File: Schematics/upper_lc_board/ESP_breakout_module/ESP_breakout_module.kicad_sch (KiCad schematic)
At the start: 28 parts, among them J8 USB_C_Female_USB2_Small, U1 ESP32-S3-WROOM-1-N16R2, U2 CAN_TRX_SN65HVD230DR, U3 PD_D3V3XA4B10LP

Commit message: finish adding components to layout, revise layout next.
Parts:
- removed C4: 0.1uF, Capacitor_SMD:C_0603_1608Metric, symbol Device:C
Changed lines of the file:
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@@
 	(wire
 		(pts
-			(xy 134.62 83.82) (xy 134.62 82.55)
-		)
-		(stroke
-			(width 0)
-			(type default)
-			(color 194 0 0 1)
-		)
-	)
-	(wire
-		(pts
 			(xy 201.93 80.01) (xy 208.28 80.01)
 		)
@@
 	)
 	(symbol
-		(lib_id "Device:C")
-		(at 134.62 78.74 0)
-		(unit 1)
-		(exclude_from_sim no)
-		(in_bom yes)
-		(on_board yes)
-		(dnp no)
-		(property "Reference" "C4"
-			(at 127.762 77.724 0)
-			(effects
-				(font
-					(size 1.27 1.27)
-				)
-				(justify left)
-			)
-		)
-		(property "Value" "0.1uF"
-			(at 127 79.7561 0)
-			(effects
-				(font
-					(size 1.27 1.27)
-				)
-				(justify left)
-			)
-		)
-		(property "Footprint" "Capacitor_SMD:C_0603_1608Metric"
-			(at 135.5852 82.55 0)
-			(effects
-				(font
-					(size 1.27 1.27)
-				)
-				(hide yes)
-			)
-		)
-		(property "Datasheet" "~"
-			(at 134.62 78.74 0)
-			(effects
-				(font
-					(size 1.27 1.27)
-				)
-				(hide yes)
-			)
-		)
-		(property "Description" "Unpolarized capacitor"
-			(at 134.62 78.74 0)
-			(effects
-				(font
-					(size 1.27 1.27)
-				)
-				(hide yes)
-			)
-		)
-		(pin "2"
-		)
-		(pin "1"
-		)
-		(instances
-			(project ""
-				(path "/9b1a1d2a-fad7-4f10-83f3-1f83e9656c75/1d6cfe1a-a78a-448d-9dfa-b2b78f04d682"
-					(reference "C4")
-					(unit 1)
-				)
-			)
-		)
-	)
-	(symbol
-		(lib_id "power:GND")
-		(at 134.62 74.93 180)
-		(unit 1)
-		(exclude_from_sim no)
-		(in_bom yes)
-		(on_board yes)
-		(dnp no)
-		(property "Reference" "#PWR013"
-			(at 134.62 68.58 0)
-			(effects
-				(font
-					(size 1.27 1.27)
-				)
-				(hide yes)
-			)
-		)
-		(property "Value" "GND"
-			(at 134.62 71.882 90)
-			(effects
-				(font
-					(size 1.27 1.27)
-				)
-				(justify right)
-			)
-		)
-		(property "Footprint" ""
-			(at 134.62 74.93 0)
-			(effects
-				(font
-					(size 1.27 1.27)
-				)
-				(hide yes)
-			)
-		)
-		(property "Datasheet" ""
-			(at 134.62 74.93 0)
-			(effects
-				(font
-					(size 1.27 1.27)
-				)
-				(hide yes)
-			)
-		)
-		(property "Description" "Power symbol creates a global label with name \"GND\" , ground"
-			(at 134.62 74.93 0)
-			(effects
-				(font
-					(size 1.27 1.27)
-				)
-				(hide yes)
-			)
-		)
-		(pin "1"
-		)
-		(instances
-			(project ""
-				(path "/9b1a1d2a-fad7-4f10-83f3-1f83e9656c75/1d6cfe1a-a78a-448d-9dfa-b2b78f04d682"
-					(reference "#PWR013")
-					(unit 1)
-				)
-			)
-		)
-	)
-	(symbol
 		(lib_id "Device:R")
 		(at 190.5 68.58 90)
@@
 					(unit 1)
 				)
-			)
-		)
-	)
-	(symbol
-		(lib_id "power:+3V3")
-		(at 134.62 83.82 180)
-		(unit 1)
-		(exclude_from_sim no)
-		(in_bom yes)
-		(on_board yes)
-		(dnp no)
-		(property "Reference" "#PWR012"
-			(at 134.62 80.01 0)
-			(effects
-				(font
-					(size 1.27 1.27)
-				)
-				(hide yes)
-			)
-		)
-		(property "Value" "+3V3"
-			(at 134.62 88.9 90)
-			(effects
-				(font
-					(size 1.27 1.27)
-				)
-			)
-		)
-		(property "Footprint" ""
-			(at 134.62 83.82 0)
-			(effects
-				(font
-					(size 1.27 1.27)
-				)
-				(hide yes)
-			)
-		)
-		(property "Datasheet" ""
-			(at 134.62 83.82 0)
-			(effects
-				(font
-					(size 1.27 1.27)
-				)
-				(hide yes)
-			)
-		)
-		(property "Description" "Power symbol creates a global label with name \"+3V3\""
-			(at 134.62 83.82 0)
-			(effects
-				(font
-					(size 1.27 1.27)
-				)
-				(hide yes)
-			)
-		)
-		(pin "1"
-		)
-		(instances
-			(project ""
-				(path "/9b1a1d2a-fad7-4f10-83f3-1f83e9656c75/1d6cfe1a-a78a-448d-9dfa-b2b78f04d682"
-					(reference "#PWR012")
-					(unit 1)
-				)

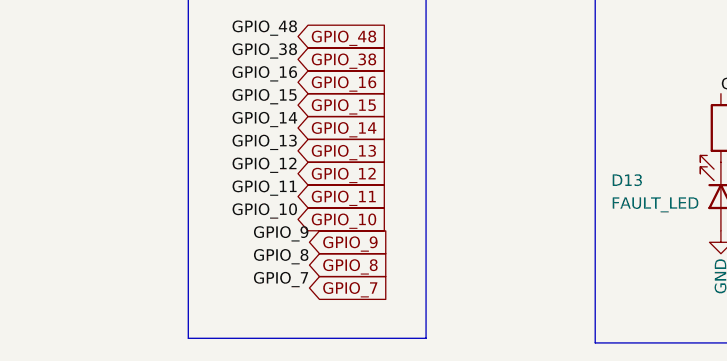
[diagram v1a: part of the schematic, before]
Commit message: add thermistor circuitry & update layout
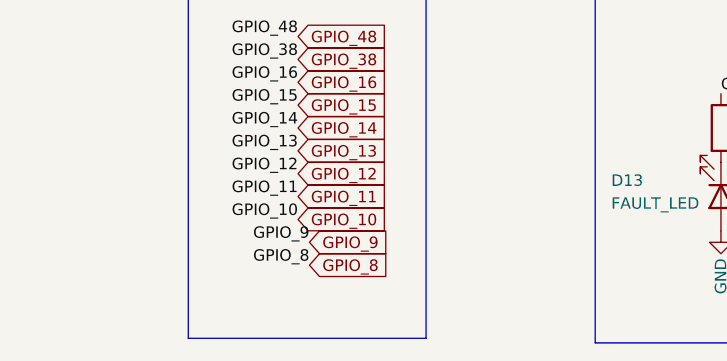
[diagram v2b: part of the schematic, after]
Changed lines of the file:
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@@
-		)
-	)
-	(label "GPIO_7"
-		(at 41.91 170.18 180)
-		(fields_autoplaced yes)
-		(effects
-			(font
-				(size 1.27 1.27)
-			)
-			(justify right bottom)
 		)
 	)
@@
 			(effects
 				(font
-					(size 1.27 1.27)
-				)
-				(justify left)
-				(hide yes)
-			)
-		)
-	)
-	(global_label "GPIO_7"
-		(shape input)
-		(at 41.91 170.18 0)
-		(fields_autoplaced yes)
-		(effects
-			(font
-				(size 1.27 1.27)
-			)
-			(justify left)
-		)
-		(property "Intersheetrefs" "${INTERSHEET_REFS}"
-			(at 51.5476 170.18 0)
-			(effects
-				(font

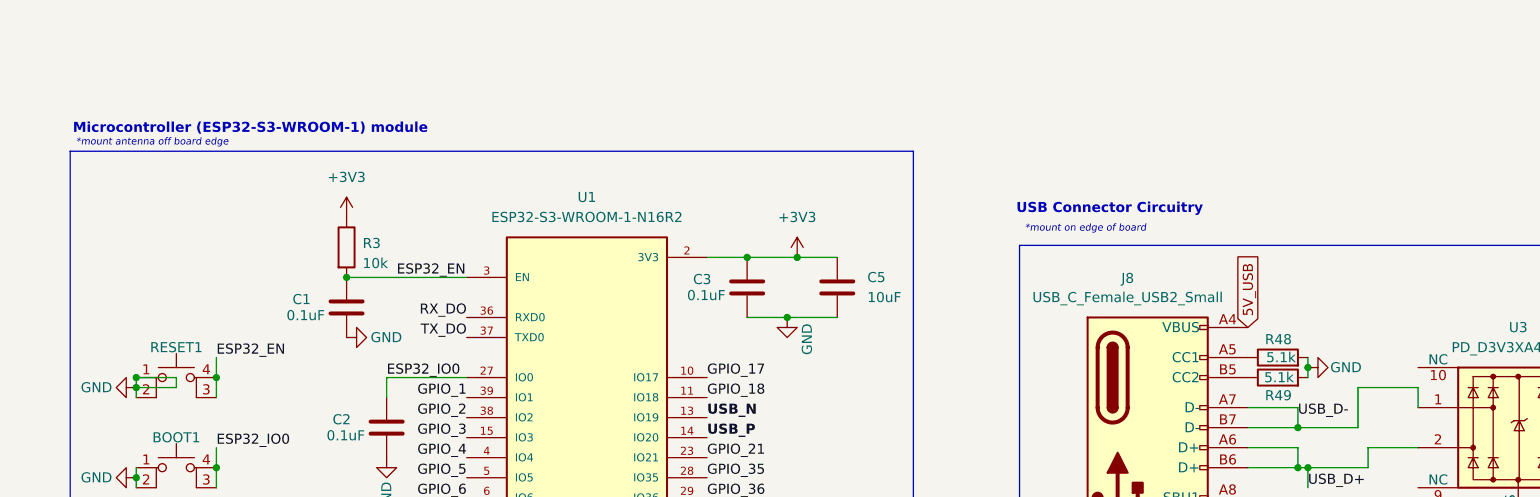
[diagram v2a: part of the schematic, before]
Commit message: add testing points throughout board schematic
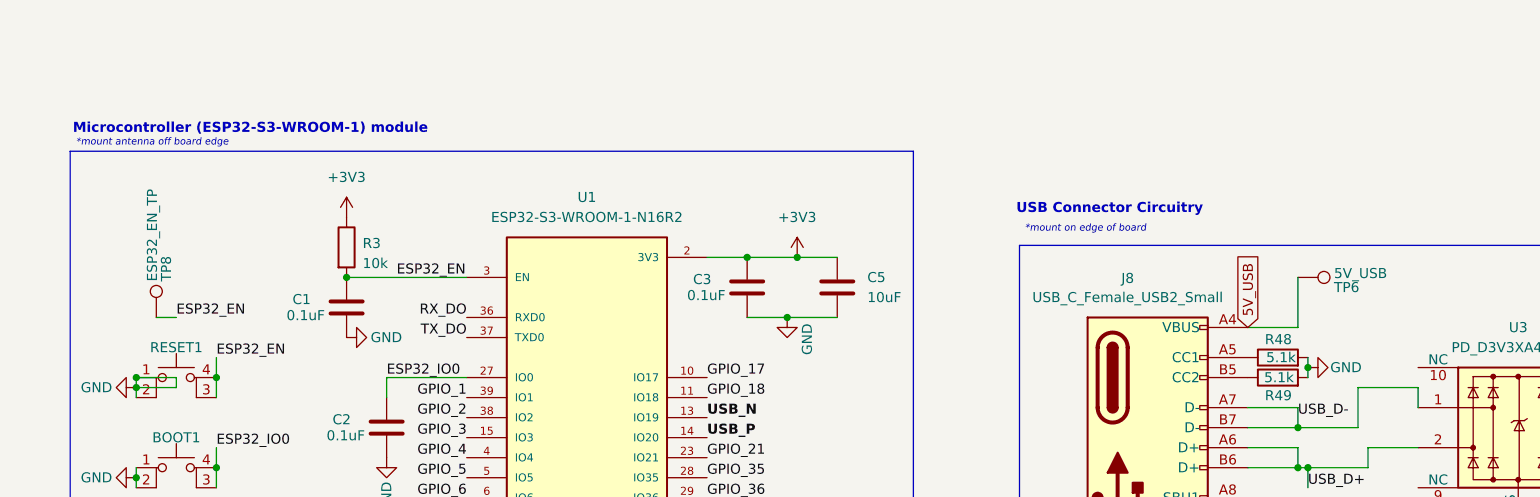
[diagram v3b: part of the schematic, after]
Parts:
- added TP6: 5V_USB, TestPoint:TestPoint_Pad_1.0x1.0mm, symbol Connector:TestPoint
- added TP8: ESP32_EN_TP, TestPoint:TestPoint_Pad_1.0x1.0mm, symbol Connector:TestPoint
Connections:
- net 5V_USB: now also TP6.1
- net ESP32_EN: now also TP8.1
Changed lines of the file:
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@@
+	(wire
+		(pts
+			(xy 48.26 63.5) (xy 50.8 63.5)
+		)
+		(stroke
+			(width 0)
+			(type default)
+		)
+	)
 	(wire
 		(pts
@@
 	(wire
 		(pts
+			(xy 193.04 64.77) (xy 193.04 58.42)
+		)
+		(stroke
+			(width 0)
+			(type default)
+		)
+	)
+	(wire
+		(pts
 			(xy 194.31 68.58) (xy 194.31 69.85)
 		)
@@
 		(pts
 			(xy 255.27 125.73) (xy 255.27 137.16)
+		)
+		(stroke
+			(width 0)
+			(type default)
+		)
+	)
+	(wire
+		(pts
+			(xy 186.69 64.77) (xy 193.04 64.77)
 		)
 		(stroke
@@
 			)
 			(justify right bottom)
+		)
+	)
+	(label "ESP32_EN"
+		(at 50.8 63.5 0)
+		(fields_autoplaced yes)
+		(effects
+			(font
+				(size 1.27 1.27)
+			)
+			(justify left bottom)
 		)
 	)
@@
 	)
 	(symbol
+		(lib_id "Connector:TestPoint")
+		(at 193.04 58.42 270)
+		(unit 1)
+		(exclude_from_sim no)
+		(in_bom yes)
+		(on_board yes)
+		(dnp no)
+		(property "Reference" "TP6"
+			(at 197.612 59.69 90)
+			(effects
+				(font
+					(size 1.27 1.27)
+				)
+				(justify left)
+			)
+		)
+		(property "Value" "5V_USB"
+			(at 197.612 57.912 90)
+			(effects
+				(font
+					(size 1.27 1.27)
+				)
+				(justify left)
+			)
+		)
+		(property "Footprint" "TestPoint:TestPoint_Pad_1.0x1.0mm"
+			(at 193.04 63.5 0)
+			(effects
+				(font
+					(size 1.27 1.27)
+				)
+				(hide yes)
+			)
+		)
+		(property "Datasheet" "~"
+			(at 193.04 63.5 0)
+			(effects
+				(font
+					(size 1.27 1.27)
+				)
+				(hide yes)
+			)
+		)
+		(property "Description" "test point"
+			(at 193.04 58.42 0)
+			(effects
+				(font
+					(size 1.27 1.27)
+				)
+				(hide yes)
+			)
+		)
+		(pin "1"
+		)
+		(instances
+			(project "upper_lc_board"
+				(path "/9b1a1d2a-fad7-4f10-83f3-1f83e9656c75/1d6cfe1a-a78a-448d-9dfa-b2b78f04d682"
+					(reference "TP6")
+					(unit 1)
+				)
+			)
+		)
+	)
+	(symbol
 		(lib_id "power:+3V3")
 		(at 236.22 74.93 0)
@@
 					(unit 1)
 				)
+			)
+		)
+	)
+	(symbol
+		(lib_id "Connector:TestPoint")
+		(at 48.26 63.5 0)
+		(unit 1)
+		(exclude_from_sim no)
+		(in_bom yes)
+		(on_board yes)
+		(dnp no)
+		(property "Reference" "TP8"
+			(at 49.53 58.928 90)
+			(effects
+				(font
+					(size 1.27 1.27)
+				)
+				(justify left)
+			)
+		)
+		(property "Value" "ESP32_EN_TP"
+			(at 47.752 58.928 90)
+			(effects
+				(font
+					(size 1.27 1.27)
+				)
+				(justify left)
+			)
+		)
+		(property "Footprint" "TestPoint:TestPoint_Pad_1.0x1.0mm"
+			(at 53.34 63.5 0)
+			(effects
+				(font
+					(size 1.27 1.27)
+				)
+				(hide yes)
+			)
+		)
+		(property "Datasheet" "~"
+			(at 53.34 63.5 0)
+			(effects
+				(font
+					(size 1.27 1.27)
+				)
+				(hide yes)
+			)
+		)
+		(property "Description" "test point"
+			(at 48.26 63.5 0)
+			(effects
+				(font
+					(size 1.27 1.27)
+				)
+				(hide yes)
+			)
+		)
+		(pin "1"
+		)
+		(instances
+			(project "upper_lc_board"
+				(path "/9b1a1d2a-fad7-4f10-83f3-1f83e9656c75/1d6cfe1a-a78a-448d-9dfa-b2b78f04d682"
+					(reference "TP8")
+					(unit 1)
+				)

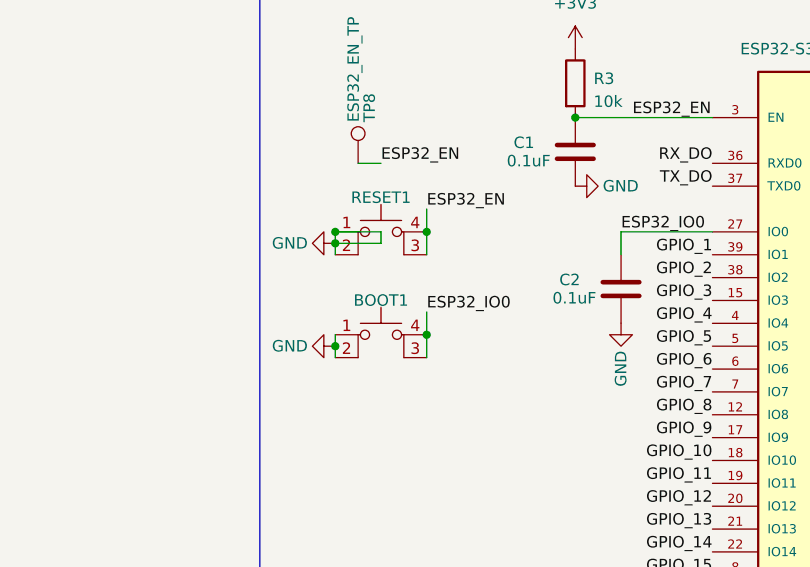
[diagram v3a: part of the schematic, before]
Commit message: fix button footprint issue
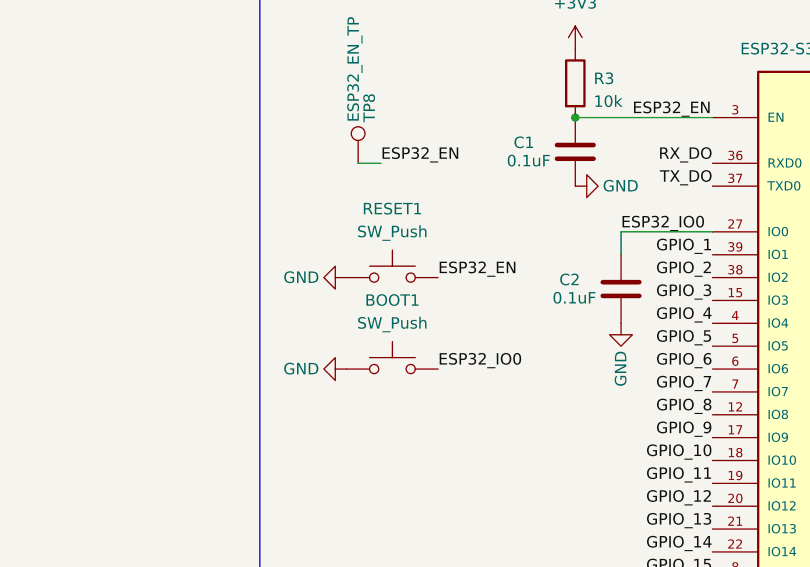
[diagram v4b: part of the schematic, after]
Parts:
- removed BOOT1: BOOT, Button_Switch_SMD:SW_Push_1P1T_XKB_TS-1187A, symbol Switch:SW_MEC_5E
- removed RESET1: Reset, Button_Switch_SMD:SW_Push_1P1T_XKB_TS-1187A, symbol Switch:SW_MEC_5E
- added BOOT1, RESET1: SW_Push, Button_Switch_SMD:SW_Push_1P1T_XKB_TS-1187A, symbol Switch:SW_Push
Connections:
- net ESP32_EN: now also RESET1.2
- net ESP32_IO0: now also BOOT1.2
- net GND: now also BOOT1.1, RESET1.1

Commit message: fix shunt resistor, add test point to layout
- sync issue with backplane connector footprint
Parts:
- TP6, TP8: footprint TestPoint:TestPoint_Pad_1.0x1.0mm -> TestPoint:TestPoint_Pad_D1.0mm
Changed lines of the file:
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@@
 			)
 		)
-		(property "Footprint" "TestPoint:TestPoint_Pad_1.0x1.0mm"
+		(property "Footprint" "TestPoint:TestPoint_Pad_D1.0mm"
 			(at 193.04 63.5 0)
 			(effects
@@
 			)
 		)
-		(property "Footprint" "TestPoint:TestPoint_Pad_1.0x1.0mm"
+		(property "Footprint" "TestPoint:TestPoint_Pad_D1.0mm"
 			(at 53.34 63.5 0)
 			(effects

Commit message: routing work
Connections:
- net USB_D+ is gone; now on net USB_P: J8.A6 (D+), J8.B6 (D+), U3.2
- net USB_D- is gone; now on net USB_N: J8.A7 (D-), J8.B7 (D-), U3.1
- net GPIO_18: now also R6.1, R7.2; no longer U2.4 (RXD)
- net GPIO_21: now also U2.4 (RXD); no longer R6.1, R7.2
- net GPIO_35: now also R2.1
- net GPIO_36: now also R1.1
- net GPIO_37: now also R26.1
- net GPIO_4: no longer R2.1
- net GPIO_5: no longer R26.1
- net GPIO_6: no longer R1.1
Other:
- note added: "*make sure purchased model does NOT have octal PSRAM"

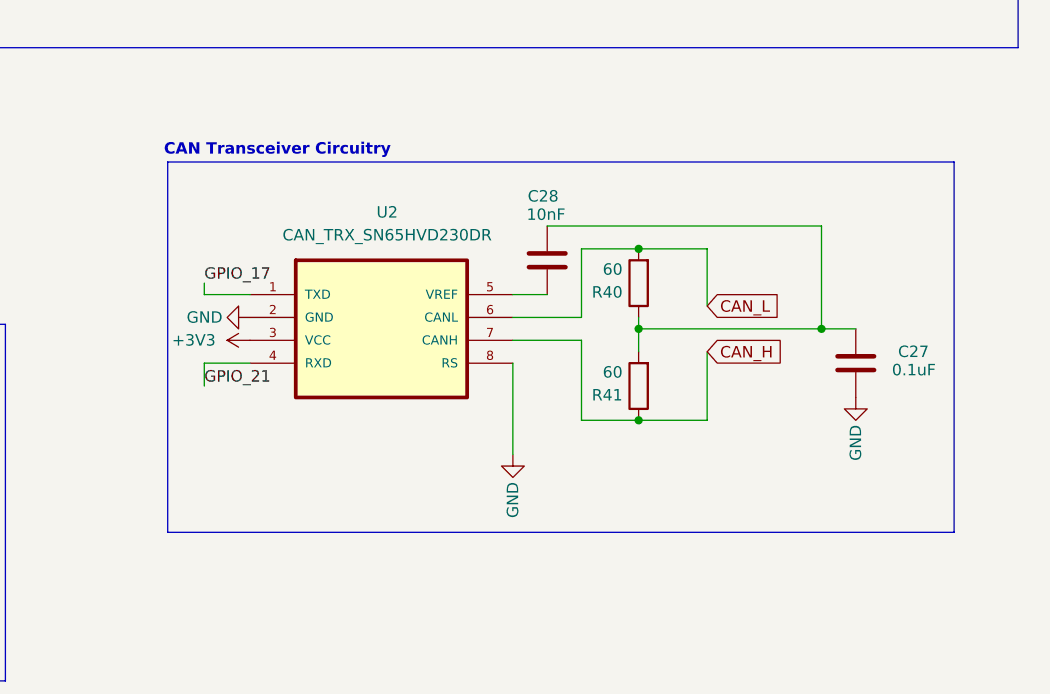
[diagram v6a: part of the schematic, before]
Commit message: fixed/updated CAN transceiver
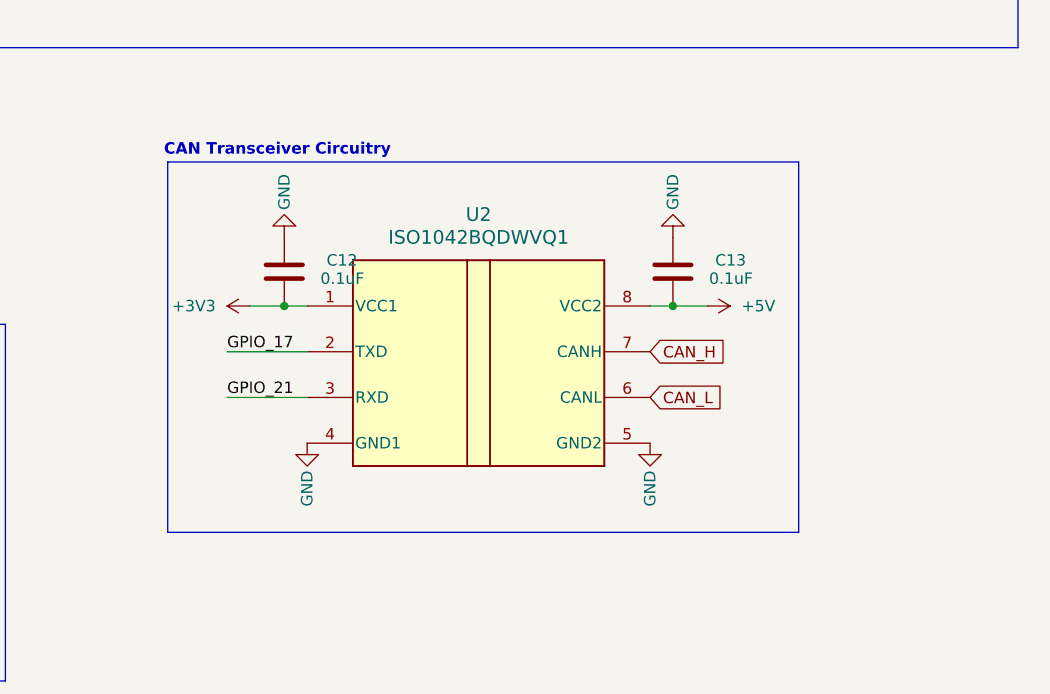
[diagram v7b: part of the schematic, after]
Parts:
- removed C27: 0.1uF, Capacitor_SMD:C_0603_1608Metric, symbol Device:C
- removed C28: 10nF, Capacitor_SMD:C_0603_1608Metric, symbol Device:C
- removed R40, R41: 60, Resistor_SMD:R_0402_1005Metric, symbol Device:R
- removed U2: CAN_TRX_SN65HVD230DR, SN65HVD230DR:SOIC127P599X175-8N, symbol SN65HVD230DR:SN65HVD230DR
- added C12, C13: 0.1uF, Capacitor_SMD:C_0603_1608Metric, symbol Device:C
- added U2: ISO1042BQDWVQ1, DWV0008A-IPC_A, symbol ISO1042BQWVQ1:ISO1042BQDWVQ1
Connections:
- net +3V3: now also C12.1, U2.1 (VCC1)
- net +5V: now also C13.1, U2.8 (VCC2)
- net CAN_H: now also U2.7 (CANH)
- net CAN_L: now also U2.6 (CANL)
- net GND: now also C12.2, C13.2, U2.4 (GND1), U2.5 (GND2)
- net GPIO_17: now also U2.2 (TXD)
- net GPIO_21: now also U2.3 (RXD)
